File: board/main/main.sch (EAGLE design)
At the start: 30 parts, among them IC1 78m05, U1 24LC256, U2 6N138M

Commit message: latest board changes
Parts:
- removed U1: 24LC256, SparkFun-IC-Memory:EEPROM-I2CSMD
- added D4, D5, D6, D7, D8, D9: SM5817, adafruit:DIODE_SOD-123FL
- added FS3: JST-PH_2-PIN_HEADER, SRG:JST-PH_2-PIN_HEADER
- added J1, J2, J3: SN49B12B, SN49B12B:SN49B12B
- added R10, R9: 100, SparkFun-Resistors:RESISTOR1206
- R5: value 10K -> 100
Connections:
- new net N$14: J1.T, R5.1
- new net N$9: J2.T, R9.1
- net FS3: now also FS3.2
- net GND: now also D5.A, D7.A, D9.A, FS3.1, J1.S, J2.S, J3.S; no longer U1.A0, U1.A1, U1.A2, U1.VSS, U1.WP
- net JACK1: now also D4.A, D5.C, R5.2
- net JACK2: now also D6.A, D7.C, R9.2
- net JACK3: now also D8.A, D9.C, R10.2
- net N$12: now also J3.T, R10.1; no longer R5.1, U1.VCC
- net SCL: no longer U1.SCL
- net SDA: no longer R5.2, U1.SDA
- net VCC: now also D4.C, D6.C, D8.C, J1.R, J2.R, J3.R
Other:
- note added: "These are in TRS format (the most common)"
- moved on the sheet: C1, C2, C3, C4, D1, D2, D3, FS1, FS1_LED, FS2, FS2_LED, IC1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

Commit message: schematic updates
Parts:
- removed D8, D9: SM5817, adafruit:DIODE_SOD-123FL
- removed PWR_LED: JST-PH_2-PIN_HEADER, SRG:JST-PH_2-PIN_HEADER
- removed R7, R8: 220, SparkFun-Resistors:RESISTOR1206
- added ACT: (no value), SparkFun-LED:LED3MM
- added C5: 0.1uF, resistor:C-EUC1206
- added FS3_LED: (no value), SparkFun-Connectors:CONN_02
- added Z1: PDZVTR5.1B, zener:PDZVTR3.0B
- FS1, FS1_LED, FS2, FS2_LED, FS3: value JST-PH_2-PIN_HEADER -> (none); device SRG:JST-PH_2-PIN_HEADER -> SparkFun-Connectors:CONN_02
- J1, J2, J3: value SN49B12B -> ACJS-MHOM; device SN49B12B:SN49B12B -> ACJS-MHOM:ACJS-MHOM
- R10: value 100 -> 1M
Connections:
- removed net N$12: J3.T, R10.1
- removed net N$4: FS1_LED.1, R7.1
- removed net N$6: FS2_LED.1, R8.1
- removed net USB_GND: MICRO.4, USB.GND
- removed net VBUS: MICRO.1, USB.VBUS
- new net N$15: C5.2, PRO_MICRO.A0
- net ACT_LED: now also R6.1; no longer PWR_LED.2
- net FS3_LED: now also FS3_LED.2
- net GND: now also ACT.C, C5.1, FS1_LED.1, FS2_LED.1, FS3_LED.1, J1.EARTH, J1.TIP-NORM, J2.EARTH, J2.TIP-NORM, J3.EARTH, J3.TIP-NORM, R10.1, Z1.A; no longer D9.A, J1.S, J2.S, J3.S, R6.2, R7.2, R8.2
- net JACK3: now also J3.TIP, Z1.K; no longer D8.A, D9.C
- net N$1: now also ACT.A, R6.2; no longer PWR_LED.1, R6.1
- net N$14: now also J1.TIP; no longer J1.T
- net N$9: now also J2.TIP; no longer J2.T
- net VCC: now also J1.RING, J2.RING; no longer D8.C, J1.R, J2.R, J3.R
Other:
- moved on the sheet: D1, D3, FS1, FS1_LED, FS2, FS2_LED, FS3, MIDI_IN, MIDI_OUT, R1, R10, R2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

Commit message: updating components
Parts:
- PWR: value DCJ0202 -> PJ-066A; device con-jack:DCJ0202 -> PJ-066A:PJ-066A
- renumbered J1 to EXP1, J2 to EXP2, J3 to TRIG
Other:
- note added: "A"
- note added: "D. Kadrioski"
- note added: "ZDS Shifter Pro"
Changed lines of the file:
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@@
 </variantdefs>
 <classes>
-<class number="0" name="default" width="0.4064" drill="0">
+<class number="0" name="default" width="0.254" drill="0">
 </class>
-<class number="2" name="GND" width="0.6096" drill="0">
+<class number="1" name="VCC" width="0.6" drill="0">
+</class>
+<class number="2" name="GND" width="0.6" drill="0">
+</class>
+<class number="3" name="RAW" width="1" drill="0">
 </class>
 </classes>
@@
 <part name="GND1" library="supply2" library_urn="urn:adsk.eagle:library:372" deviceset="GND" device=""/>
 <part name="GND2" library="supply2" library_urn="urn:adsk.eagle:library:372" deviceset="GND" device=""/>
-<part name="PWR" library="con-jack" deviceset="DCJ0202" device="" value="DCJ0202"/>
+<part name="PWR" library="PJ-066A" deviceset="PJ-066A" device="" value="PJ-066A"/>
 <part name="MICRO" library="con-lstb" deviceset="MA04-1" device="" value="PINS"/>
 <part name="USB" library="SparkFun-Connectors" deviceset="USB_B" device="_PTH" value=""/>
@@
 <part name="GND12" library="supply2" library_urn="urn:adsk.eagle:library:372" deviceset="GND" device=""/>
 <part name="GND13" library="supply2" library_urn="urn:adsk.eagle:library:372" deviceset="GND" device=""/>
-<part name="J1" library="ACJS-MHOM" deviceset="ACJS-MHOM" device=""/>
-<part name="J2" library="ACJS-MHOM" deviceset="ACJS-MHOM" device=""/>
-<part name="J3" library="ACJS-MHOM" deviceset="ACJS-MHOM" device=""/>
+<part name="EXP1" library="ACJS-MHOM" deviceset="ACJS-MHOM" device=""/>
+<part name="EXP2" library="ACJS-MHOM" deviceset="ACJS-MHOM" device=""/>
+<part name="TRIG" library="ACJS-MHOM" deviceset="ACJS-MHOM" device=""/>
 <part name="C5" library="resistor" library_urn="urn:adsk.eagle:library:348" deviceset="C-EU" device="C1206" package3d_urn="urn:adsk.eagle:package:23618/2" value="0.1uF"/>
 <part name="GND14" library="supply2" library_urn="urn:adsk.eagle:library:372" deviceset="GND" device=""/>
@@
 <plain>
 <text x="17.78" y="162.56" size="1.778" layer="91">These are in TRS format (the most common)</text>
+<text x="186.436" y="21.336" size="2.54" layer="91">ZDS Shifter Pro</text>
+<text x="231.648" y="11.43" size="2.54" layer="91">D. Kadrioski</text>
+<text x="240.03" y="6.35" size="2.54" layer="91">A</text>
 </plain>
 <instances>
@@
 <attribute name="VALUE" x="35.56" y="53.34" size="1.778" layer="96"/>
 </instance>
-<instance part="J1" gate="G$1" x="17.78" y="149.86" smashed="yes" rot="MR180">
+<instance part="EXP1" gate="G$1" x="17.78" y="149.86" smashed="yes" rot="MR180">
 <attribute name="NAME" x="12.7" y="141.732" size="1.778" layer="95" rot="MR180"/>
 <attribute name="VALUE" x="12.7" y="157.48" size="1.778" layer="96" rot="MR180"/>
 </instance>
-<instance part="J2" gate="G$1" x="17.78" y="114.3" smashed="yes" rot="MR180">
+<instance part="EXP2" gate="G$1" x="17.78" y="114.3" smashed="yes" rot="MR180">
 <attribute name="NAME" x="12.7" y="106.172" size="1.778" layer="95" rot="MR180"/>
 <attribute name="VALUE" x="12.7" y="121.92" size="1.778" layer="96" rot="MR180"/>
 </instance>
-<instance part="J3" gate="G$1" x="17.78" y="81.28" smashed="yes" rot="MR180">
+<instance part="TRIG" gate="G$1" x="17.78" y="81.28" smashed="yes" rot="MR180">
 <attribute name="NAME" x="12.7" y="73.152" size="1.778" layer="95" rot="MR180"/>
 <attribute name="VALUE" x="12.7" y="88.9" size="1.778" layer="96" rot="MR180"/>
@@
 <wire x1="147.32" y1="132.08" x2="147.32" y2="144.78" width="0.1524" layer="91"/>
 <pinref part="PWR" gate="G$1" pin="3"/>
-<wire x1="99.06" y1="147.32" x2="101.6" y2="147.32" width="0.1524" layer="91"/>
-<wire x1="101.6" y1="147.32" x2="101.6" y2="132.08" width="0.1524" layer="91"/>
+<wire x1="96.52" y1="149.86" x2="101.6" y2="149.86" width="0.1524" layer="91"/>
+<wire x1="101.6" y1="149.86" x2="101.6" y2="132.08" width="0.1524" layer="91"/>
 <wire x1="101.6" y1="132.08" x2="119.38" y2="132.08" width="0.1524" layer="91"/>
 <junction x="147.32" y="132.08"/>
@@
 <wire x1="38.1" y1="137.16" x2="38.1" y2="134.62" width="0.1524" layer="91"/>
 <junction x="38.1" y="137.16"/>
-<pinref part="J1" gate="G$1" pin="EARTH"/>
-<pinref part="J1" gate="G$1" pin="TIP-NORM"/>
+<pinref part="EXP1" gate="G$1" pin="EARTH"/>
+<pinref part="EXP1" gate="G$1" pin="TIP-NORM"/>
 <wire x1="30.48" y1="142.24" x2="30.48" y2="149.86" width="0.1524" layer="91"/>
 <wire x1="30.48" y1="149.86" x2="22.86" y2="149.86" width="0.1524" layer="91"/>
@@
 <wire x1="38.1" y1="101.6" x2="38.1" y2="99.06" width="0.1524" layer="91"/>
 <junction x="38.1" y="101.6"/>
-<pinref part="J2" gate="G$1" pin="EARTH"/>
+<pinref part="EXP2" gate="G$1" pin="EARTH"/>
 <wire x1="38.1" y1="106.68" x2="30.48" y2="106.68" width="0.1524" layer="91"/>
-<pinref part="J2" gate="G$1" pin="TIP-NORM"/>
+<pinref part="EXP2" gate="G$1" pin="TIP-NORM"/>
 <wire x1="30.48" y1="106.68" x2="22.86" y2="106.68" width="0.1524" layer="91"/>
 <wire x1="30.48" y1="106.68" x2="30.48" y2="114.3" width="0.1524" layer="91"/>
@@
 <wire x1="38.1" y1="63.5" x2="38.1" y2="58.42" width="0.1524" layer="91"/>
 <junction x="38.1" y="63.5"/>
-<pinref part="J3" gate="G$1" pin="EARTH"/>
-<pinref part="J3" gate="G$1" pin="TIP-NORM"/>
+<pinref part="TRIG" gate="G$1" pin="EARTH"/>
+<pinref part="TRIG" gate="G$1" pin="TIP-NORM"/>
 <wire x1="30.48" y1="73.66" x2="30.48" y2="81.28" width="0.1524" layer="91"/>
 <wire x1="30.48" y1="81.28" x2="22.86" y2="81.28" width="0.1524" layer="91"/>
@@
 </segment>
 </net>
-<net name="VCC" class="0">
+<net name="VCC" class="1">
 <segment>
 <pinref part="PRO_MICRO" gate="G$1" pin="VCC"/>
@@
 <junction x="38.1" y="157.48"/>
 <label x="35.56" y="157.48" size="1.016" layer="95" rot="R180" xref="yes"/>
-<pinref part="J1" gate="G$1" pin="RING"/>
+<pinref part="EXP1" gate="G$1" pin="RING"/>
 <wire x1="38.1" y1="152.4" x2="22.86" y2="152.4" width="0.1524" layer="91"/>
 </segment>
@@
 <junction x="38.1" y="121.92"/>
 <label x="35.56" y="121.92" size="1.016" layer="95" rot="R180" xref="yes"/>
-<pinref part="J2" gate="G$1" pin="RING"/>
+<pinref part="EXP2" gate="G$1" pin="RING"/>
 <wire x1="38.1" y1="116.84" x2="22.86" y2="116.84" width="0.1524" layer="91"/>
 </segment>
@@
 <segment>
 <label x="63.5" y="78.74" size="1.016" layer="95" xref="yes"/>
-<pinref part="J3" gate="G$1" pin="TIP"/>
+<pinref part="TRIG" gate="G$1" pin="TIP"/>
 <pinref part="Z1" gate="G$1" pin="K"/>
 <wire x1="22.86" y1="78.74" x2="45.72" y2="78.74" width="0.1524" layer="91"/>
@@
 <pinref part="PWR" gate="G$1" pin="1"/>
 <pinref part="D2" gate="G$1" pin="A"/>
-<wire x1="99.06" y1="152.4" x2="106.68" y2="152.4" width="0.1524" layer="91"/>
-</segment>
-</net>
-<net name="RAW" class="0">
+<wire x1="96.52" y1="152.4" x2="106.68" y2="152.4" width="0.1524" layer="91"/>
+</segment>
+</net>
+<net name="RAW" class="3">
 <segment>
 <pinref part="PRO_MICRO" gate="G$1" pin="RAW"/>
@@
 <pinref part="R5" gate="G$1" pin="1"/>
 <wire x1="22.86" y1="147.32" x2="43.18" y2="147.32" width="0.1524" layer="91"/>
-<pinref part="J1" gate="G$1" pin="TIP"/>
+<pinref part="EXP1" gate="G$1" pin="TIP"/>
 </segment>
 </net>
@@
 <pinref part="R9" gate="G$1" pin="1"/>
 <wire x1="22.86" y1="111.76" x2="43.18" y2="111.76" width="0.1524" layer="91"/>
-<pinref part="J2" gate="G$1" pin="TIP"/>
-</segment>
-</net>
+<pinref part="EXP2" gate="G$1" pin="TIP"/>
+</segment>
+</net>

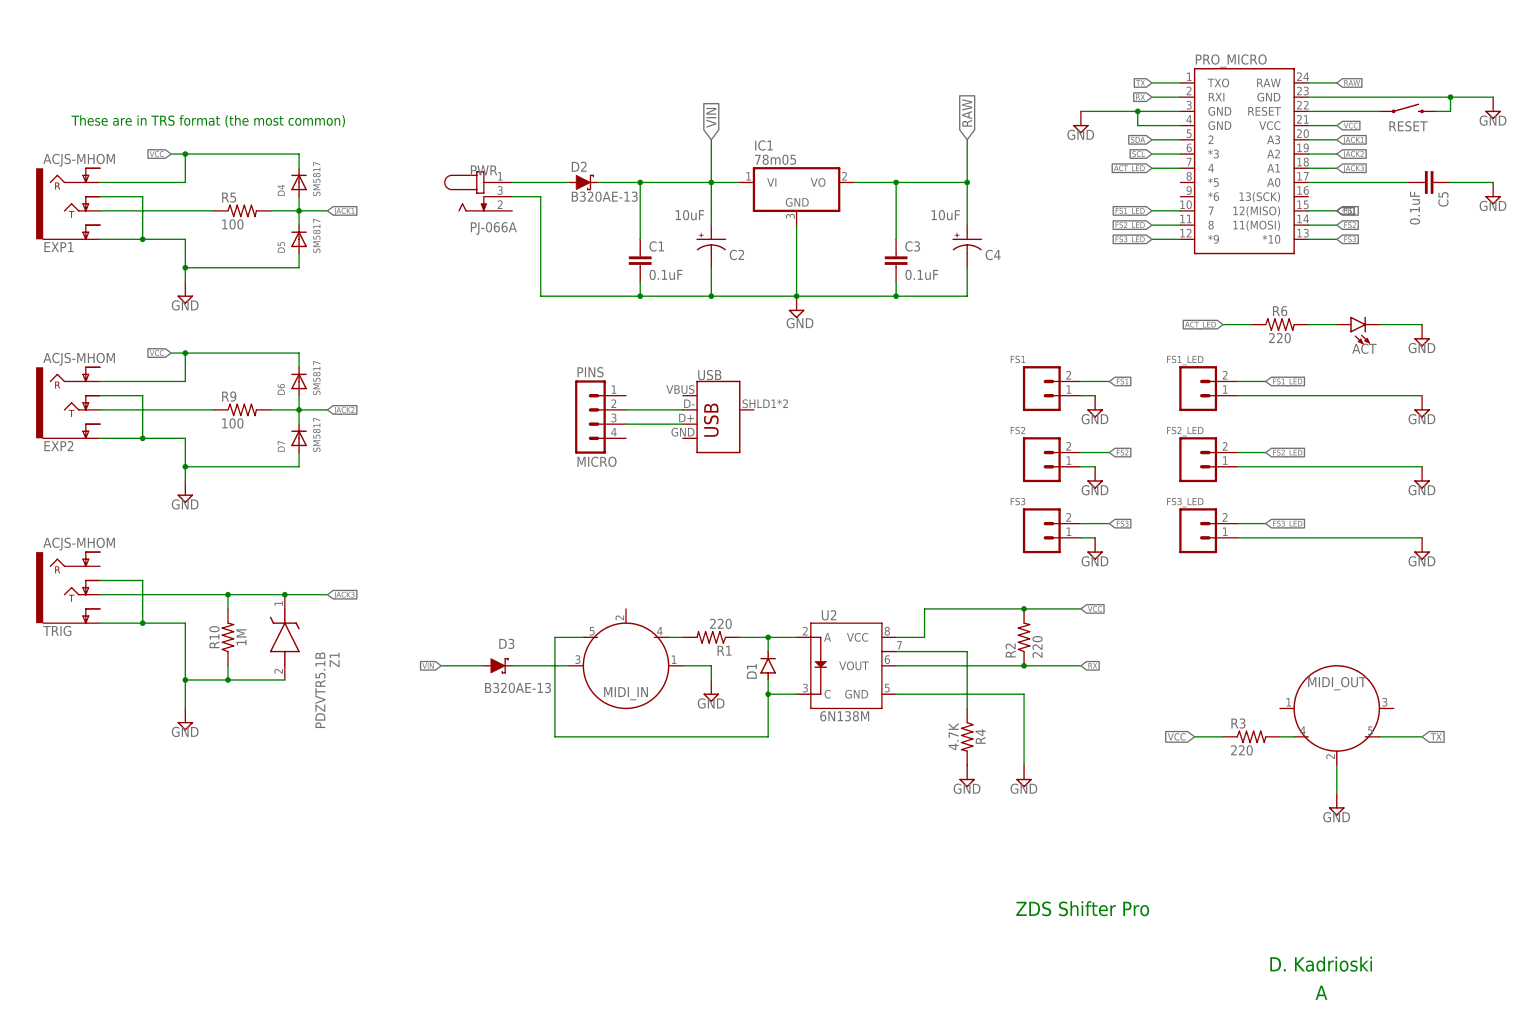
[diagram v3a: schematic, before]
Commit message: Switch to teensy (#1)
* finalized buttons

* board updates

* 3d print of button template

* code compiles for teensy successfully (still need to test)

* midi is working

* expression pedals are working

* turning on both

placing a 1K resistor between pin 16 and ground

* essentially working

* add todo

* submitting main board to jlcpcb
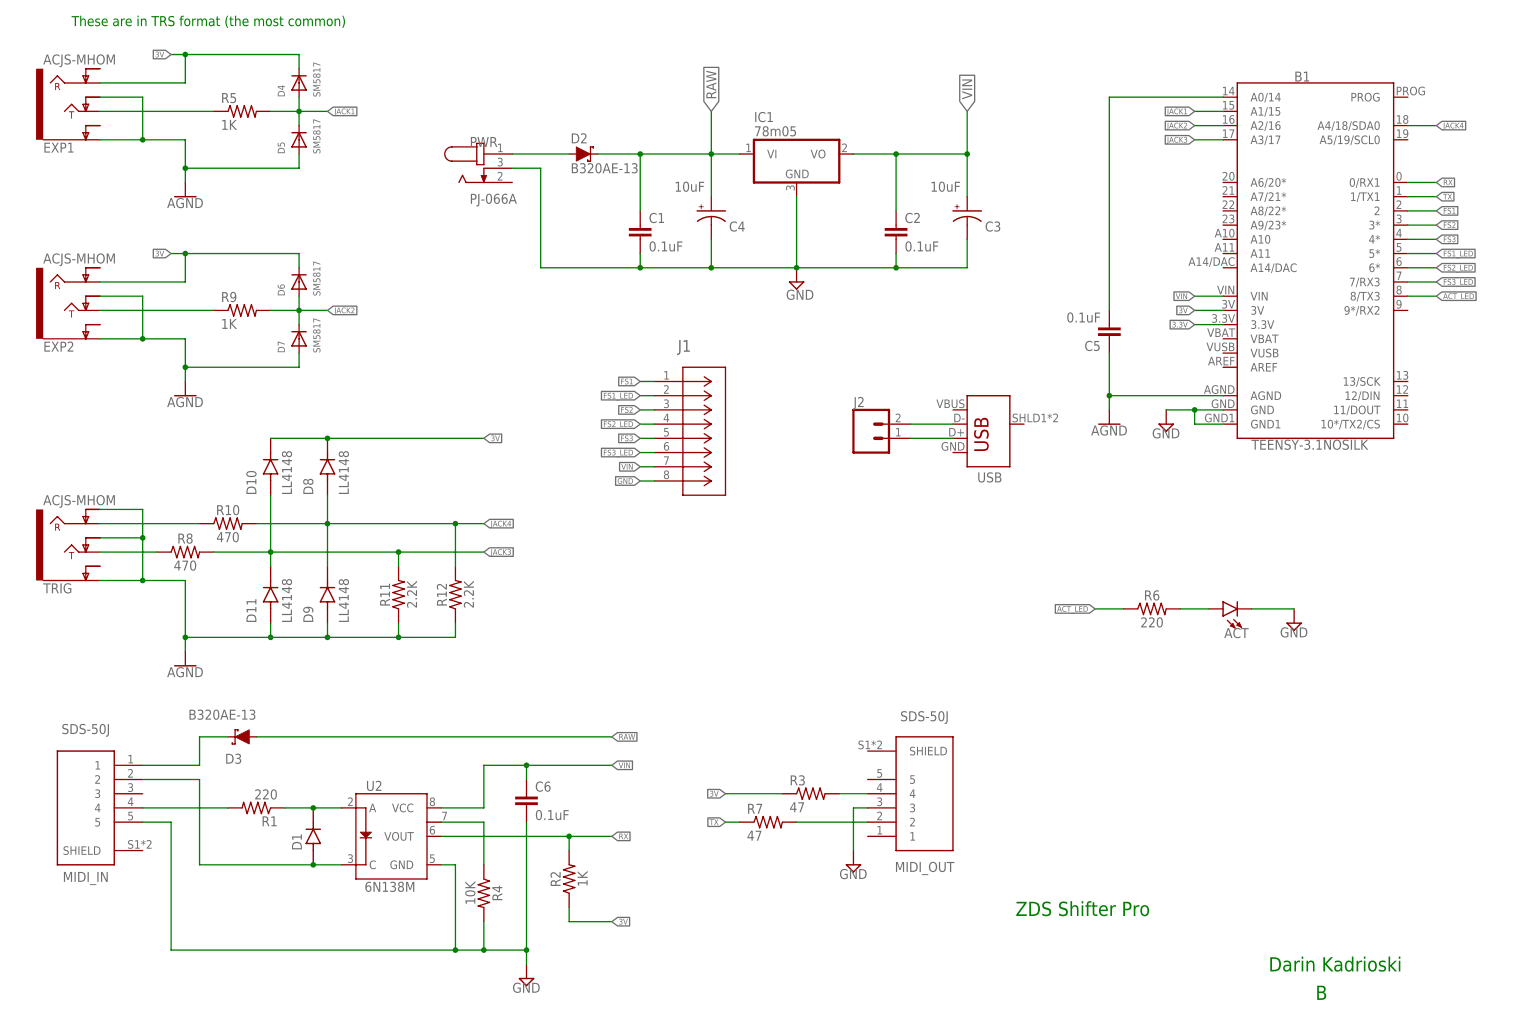
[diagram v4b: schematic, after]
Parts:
- removed FS1, FS1_LED, FS2, FS2_LED, FS3, FS3_LED: (no value), SparkFun-Connectors:CONN_02
- removed MICRO: PINS, con-lstb:MA04-1
- removed PRO_MICRO: SPARKFUN_PRO_MICRO, SparkFun-Boards:SPARKFUN_PRO_MICRO
- removed RESET: MOMENTARY-SWITCH-SPST-PTH-6.0MM, SparkFun-Switches:MOMENTARY-SWITCH-SPST-PTH-6.0MM
- removed Z1: PDZVTR5.1B, zener:PDZVTR3.0B
- added B1: TEENSY-3.1NOSILK, SparkFun-Boards:TEENSY-3.1NOSILK
- added C6: 0.1uF, resistor:C-EUC1206
- added D10, D11, D8, D9: LL4148, LL4148:LL4148
- added J1: 188275-8, ul_1882758:188275-8
- added J2: (no value), SparkFun-Connectors:CONN_02
- added R11, R12: 2.2K, SparkFun-Resistors:RESISTOR1206
- added R7: 47, SparkFun-Resistors:RESISTOR1206
- added R8: 470, SparkFun-Resistors:RESISTOR1206
- C2: value 10uF -> 0.1uF; device SparkFun-Capacitors:47UF-POLAR-PANASONIC_D-35V-20% -> resistor:C-EUC1206
- C3: value 0.1uF -> 10uF; device resistor:C-EUC1206 -> SparkFun-Capacitors:47UF-POLAR-PANASONIC_D-35V-20%
- D1: device diode:DIODE-SMC -> LL4148:LL4148
- MIDI_IN, MIDI_OUT: value DIN5 -> SDS-50J; device SparkFun-Connectors:DIN5 -> SDS-50J:SDS-50J
- R10: value 1M -> 470
- R2: value 220 -> 1K
- R3: value 220 -> 47
- R4: value 4.7K -> 10K
- R5, R9: value 100 -> 1K
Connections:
- removed net N$15: C5.2, PRO_MICRO.A0
- removed net RESET: PRO_MICRO.RESET, RESET.1
- removed net SCL: PRO_MICRO.*3
- removed net SDA: PRO_MICRO.2
- removed net VCC: D4.C, D6.C, EXP1.RING, EXP2.RING, PRO_MICRO.VCC, R2.2, R3.1, U2.VCC
- new net 3.3V: B1.3.3V
- new net 3V: B1.3V, D10.C, D4.C, D6.C, D8.C, EXP1.RING, EXP2.RING, R2.1, R3.1
- new net AGND: B1.AGND, C5.1, D11.A, D5.A, D7.A, D9.A, EXP1.EARTH, EXP1.TIP-NORM, EXP2.EARTH, EXP2.TIP-NORM, R11.1, R12.1, TRIG.EARTH, TRIG.RING-NORM, TRIG.TIP-NORM
- new net JACK4: B1.A4/18/SDA0, D8.A, D9.C, R10.2, R12.2
- new net N$12: R10.1, TRIG.RING
- new net N$4: B1.A0/14, C5.2
- new net N$6: MIDI_OUT.2, R7.2
- net ACT_LED: now also B1.8/TX3; no longer PRO_MICRO.4
- net FS1: now also B1.2, J1.1; no longer FS1.2, PRO_MICRO.12(MISO)
- net FS1_LED: now also B1.5*, J1.2; no longer FS1_LED.2, PRO_MICRO.7
- net FS2: now also B1.3*, J1.3; no longer FS2.2, PRO_MICRO.11(MOSI)
- net FS2_LED: now also B1.6*, J1.4; no longer FS2_LED.2, PRO_MICRO.8
- net FS3: now also B1.4*, J1.5; no longer FS3.2, PRO_MICRO.*10
- net FS3_LED: now also B1.7/RX3, J1.6; no longer FS3_LED.2, PRO_MICRO.*9
- net GND: now also B1.GND, B1.GND1, C2.2, C3.-, C6.2, J1.8, MIDI_IN.5, MIDI_OUT.3; no longer C2.-, C3.2, C5.1, D5.A, D7.A, EXP1.EARTH, EXP1.TIP-NORM, EXP2.EARTH, EXP2.TIP-NORM, FS1.1, FS1_LED.1, FS2.1, FS2_LED.1, FS3.1, FS3_LED.1, MIDI_IN.1, MIDI_OUT.2, PRO_MICRO.GND, PRO_MICRO.GND@1, PRO_MICRO.GND@2, R10.1, RESET.2, TRIG.EARTH, TRIG.TIP-NORM, Z1.A
- net JACK1: now also B1.A1/15; no longer PRO_MICRO.A3
- net JACK2: now also B1.A2/16; no longer PRO_MICRO.A2
- net JACK3: now also B1.A3/17, D10.A, D11.C, R11.2, R8.1, R8.2; no longer PRO_MICRO.A1, R10.2, Z1.K
- net N$10: now also J2.1; no longer MICRO.3
- net N$13: now also J2.2; no longer MICRO.2
- net N$2: now also MIDI_IN.2; no longer MIDI_IN.5
- net N$5: now also MIDI_IN.1; no longer MIDI_IN.3
- net RAW: now also C1.1, D2.C, D3.A, IC1.VI; no longer C3.1, IC1.VO, PRO_MICRO.RAW
- net RX: now also B1.0/RX1, R2.2; no longer PRO_MICRO.RXI, R2.1
- net TX: now also B1.1/TX1, R7.1; no longer MIDI_OUT.5, PRO_MICRO.TXO
- net VIN: now also B1.VIN, C2.1, C3.+, C6.1, IC1.VO, J1.7, U2.VCC; no longer C1.1, C2.+, D2.C, D3.A, IC1.VI
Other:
- note removed: "A"
- note removed: "D. Kadrioski"
- note removed: "ZDS Shifter Pro"
- moved on the sheet: ACT, C1, C4, C5, D2, D3, D4, D5, D6, D7, EXP1, EXP2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
